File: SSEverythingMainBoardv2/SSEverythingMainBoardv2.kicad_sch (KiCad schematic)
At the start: 66 parts, among them J1 CONN_06SILK_FEMALE_PTH, J2 CONN_06SILK_FEMALE_PTH, J3 POWER, J4 Switch, J5 Conn_01x02, J6 Conn_01x05, M1 Left MOTOR, M2 Right MOTOR, Q1 PBSS4160DS, Q2 PBSS4160DS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

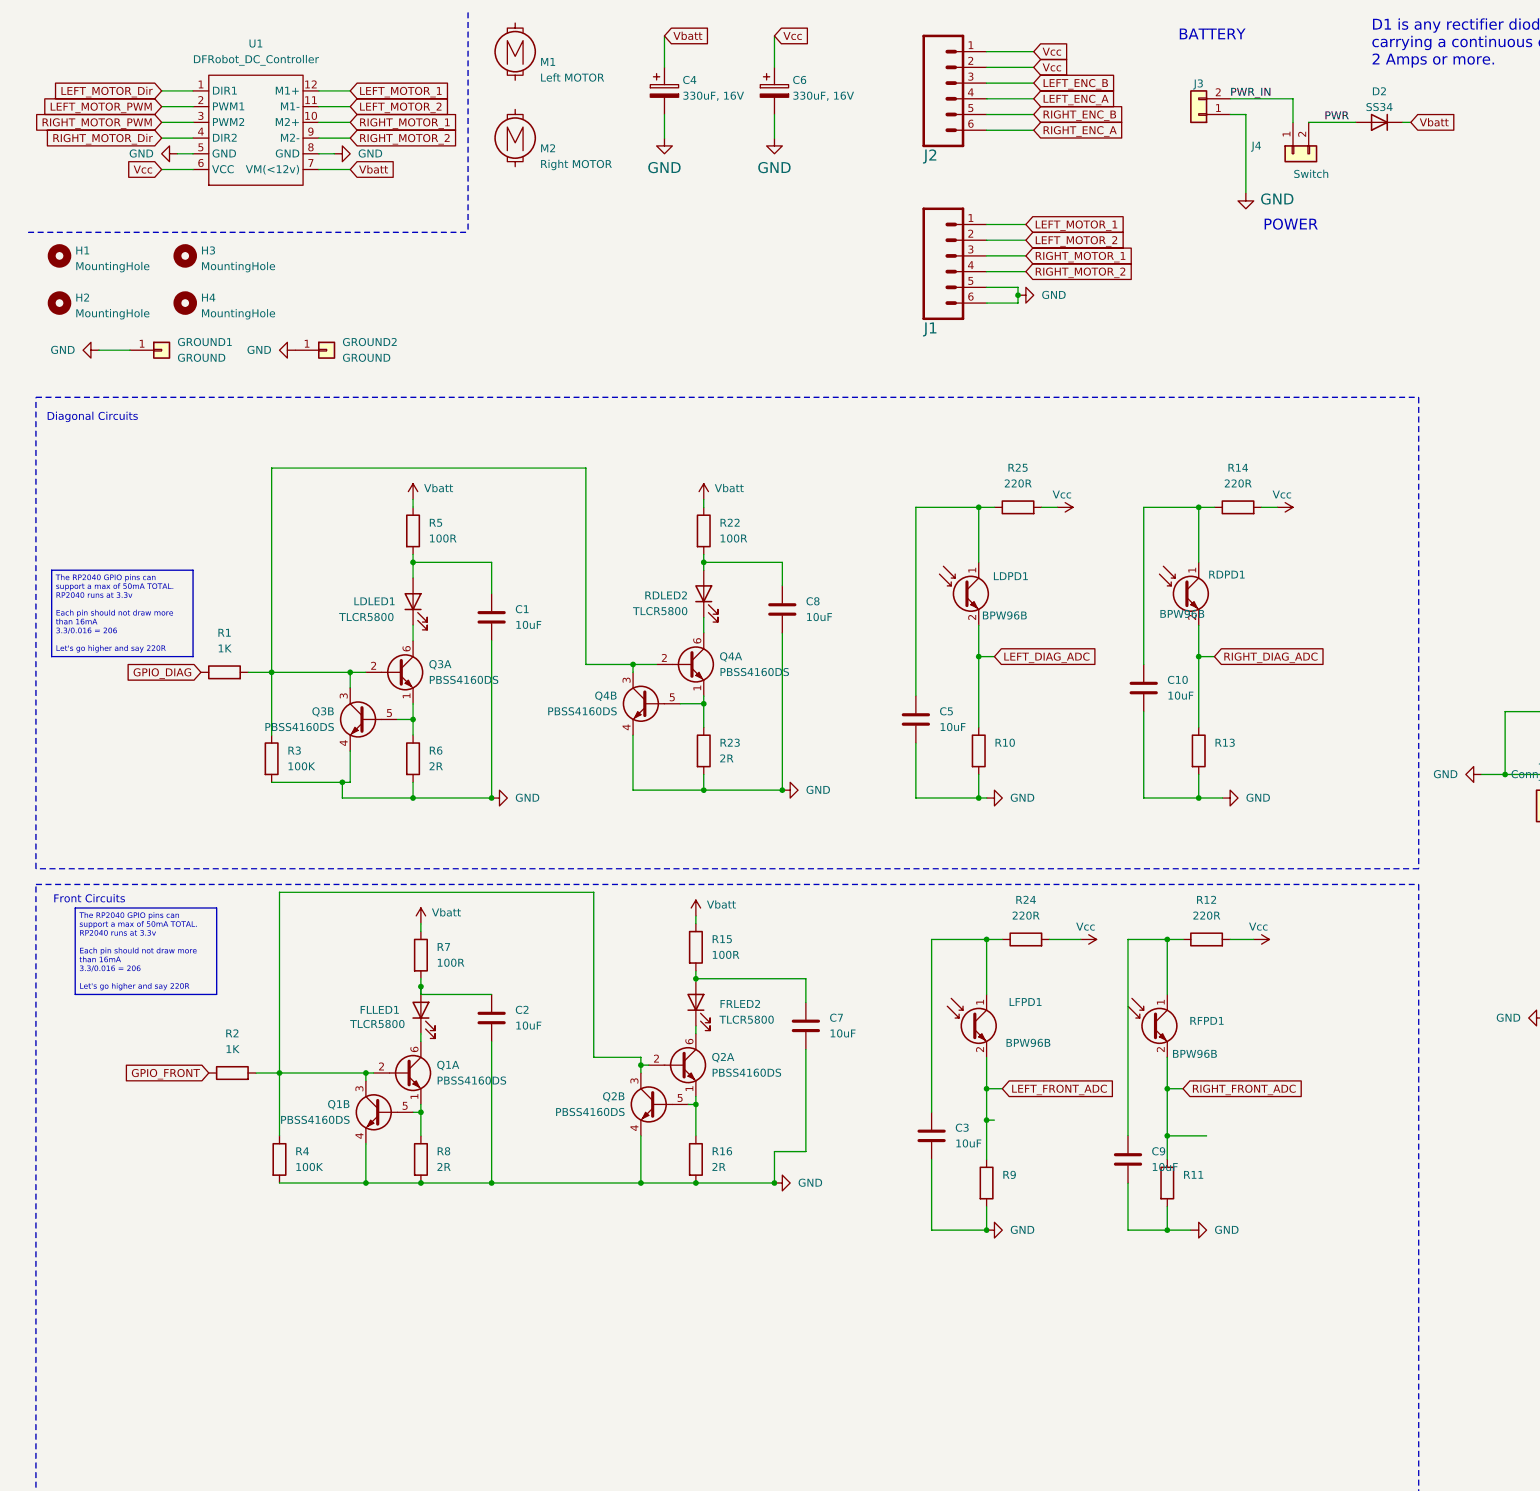
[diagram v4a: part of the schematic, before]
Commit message: updated sensor locations, all resistors are back to be 0805, routing changes and moved the motor controller around plus other changes from Peter's suggestions
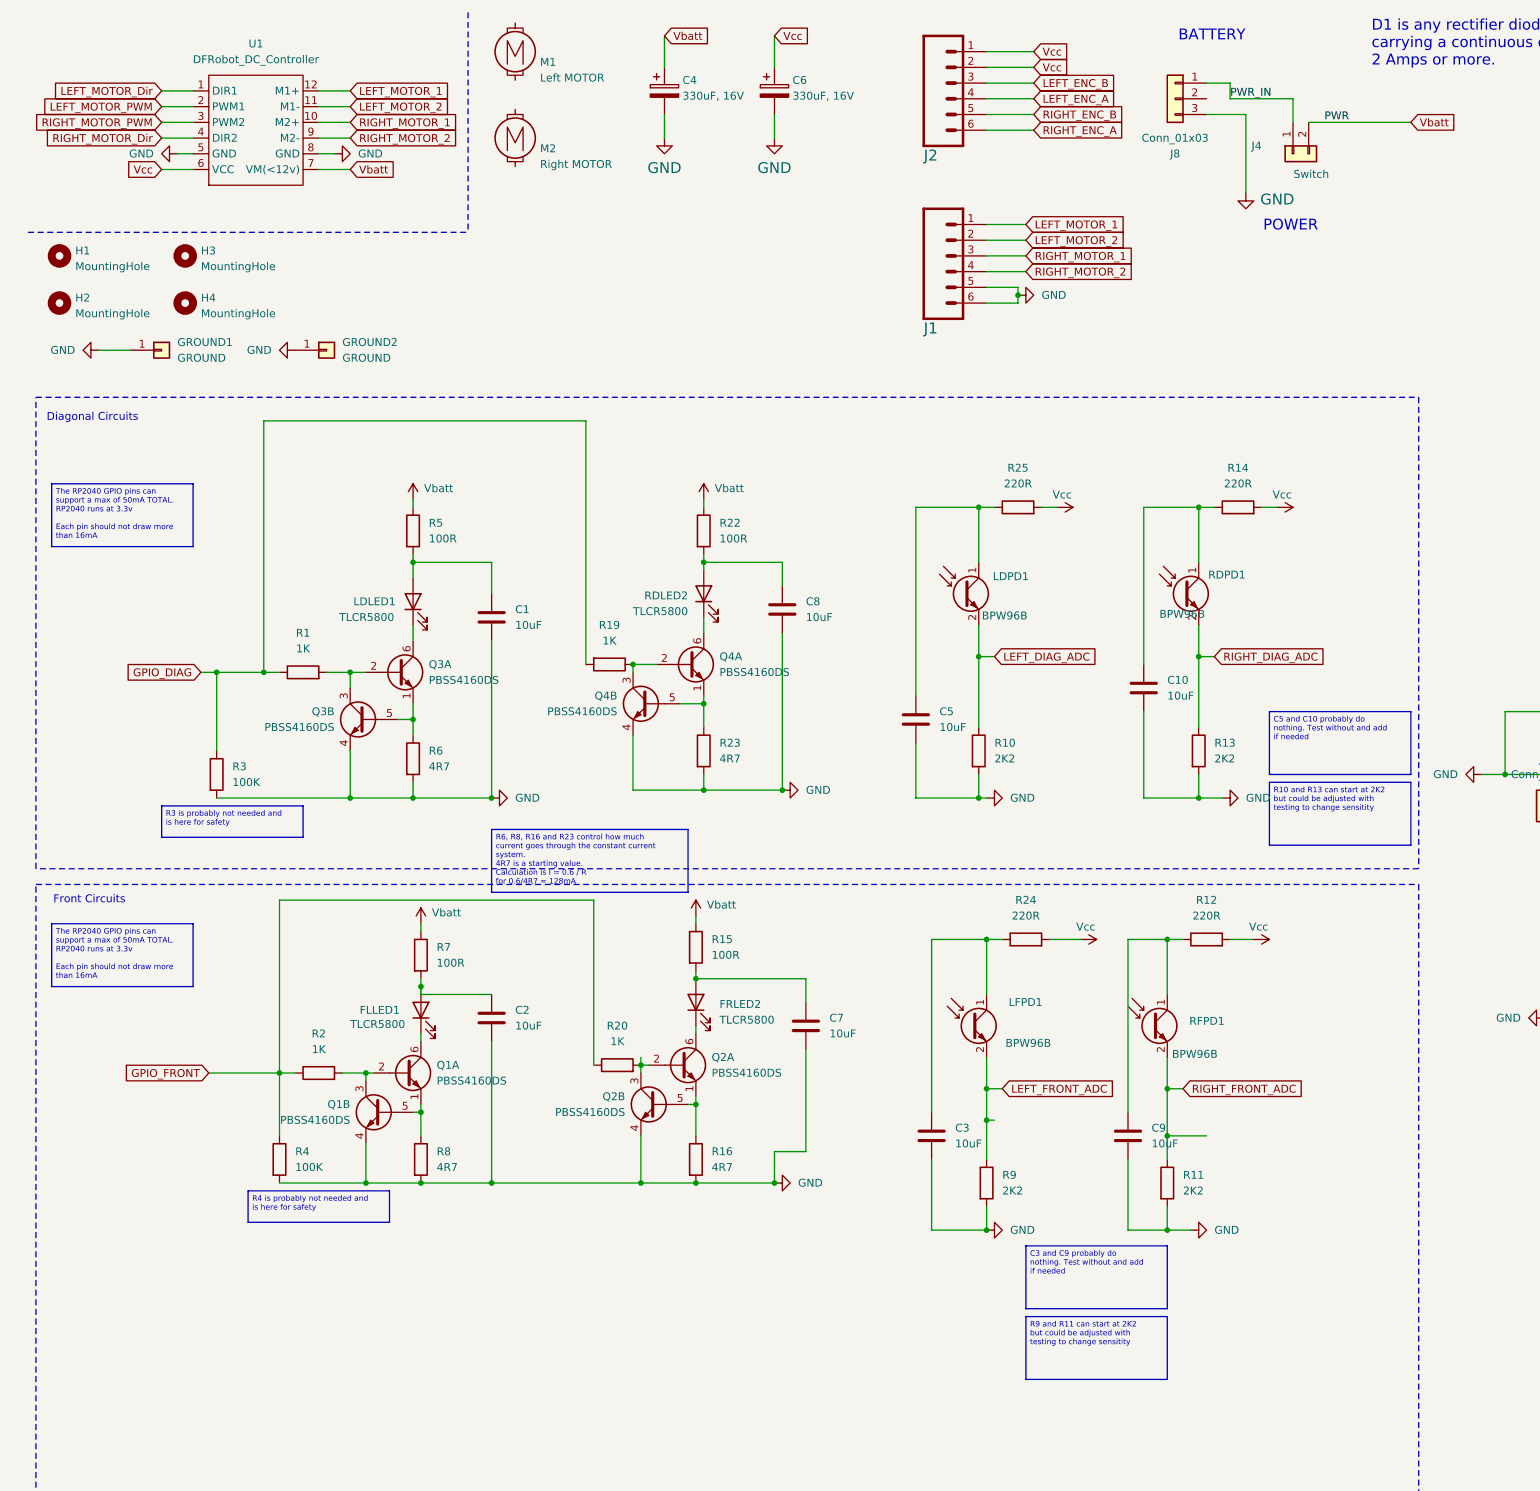
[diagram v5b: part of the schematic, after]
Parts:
- removed D2: SS34, Diode_SMD:D_SMC, symbol Device:D
- removed J3: POWER, Connector_PinHeader_2.54mm:PinHeader_1x02_P2.54mm_Vertical, symbol Connector_Generic:Conn_01x02
- added J8: Conn_01x03, Connector_JST:JST_XH_B3B-XH-A_1x03_P2.50mm_Vertical, symbol Connector_Generic:Conn_01x03
- added R19, R20: 1K, Resistor_SMD:R_0805_2012Metric_Pad1.20x1.40mm_HandSolder, symbol Device:R
- C4, C6: footprint Capacitor_THT:CP_Radial_D8.0mm_P2.50mm -> Capacitor_THT:C_Radial_D6.3mm_H7.0mm_P2.50mm
- R10, R11, R13, R9: value R -> 2K2
- R16, R23, R6, R8: value 2R -> 4R7; footprint Resistor_SMD:R_1206_3216Metric_Pad1.30x1.75mm_HandSolder -> Resistor_SMD:R_0805_2012Metric_Pad1.20x1.40mm_HandSolder
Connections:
- net PWR is gone; now on net Vbatt: J4.2 (Pin_2)
- net GND: now also J8.3 (Pin_3)
- net GPIO_DIAG: now also R3.1, R19.2
- net GPIO_FRONT: now also R4.1, R20.1
- net PWR_IN: now also J8.1 (Pin_1)
- net at Q1.2 (B1), Q1.3 (C2), R2.2: no longer Q2.2 (B1), Q2.3 (C2), R4.1
- net at Q3.2 (B1), Q3.3 (C2), R1.2: no longer Q4.2 (B1), Q4.3 (C2), R3.1
- new net: Q4.2 (B1), Q4.3 (C2), R19.1
- new net: Q2.2 (B1), Q2.3 (C2), R20.2
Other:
- moved on the sheet: C9, R1, R2, R3

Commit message: routing changes
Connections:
- net LEFT_DIAG_ADC: now also A1.19 (A0); no longer A1.20 (A1)
- net LEFT_FRONT_ADC: now also A1.20 (A1); no longer A1.19 (A0)

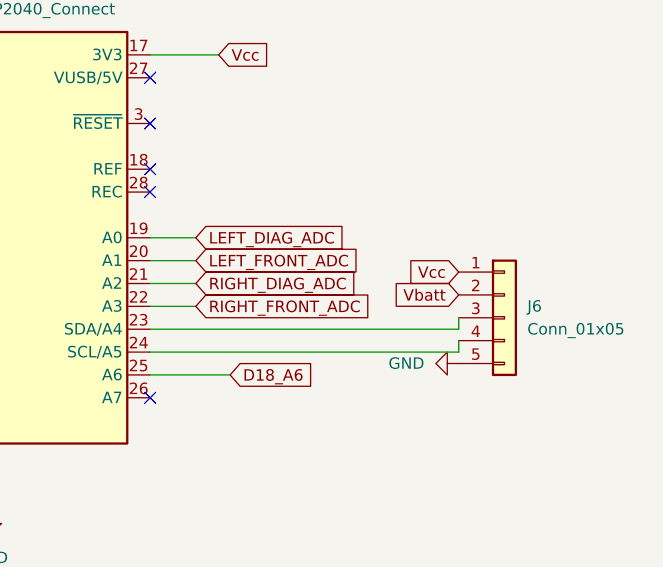
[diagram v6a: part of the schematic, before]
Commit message: New board sent to JLCPCB for new Chassis
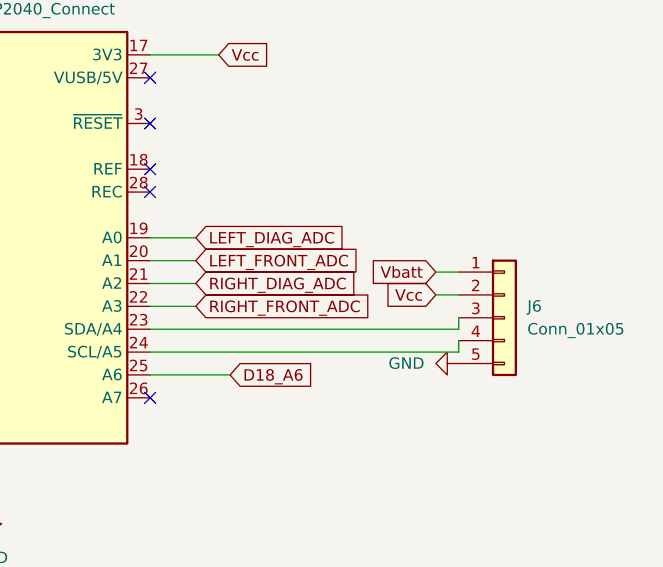
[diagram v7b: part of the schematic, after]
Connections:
- net Vbatt: now also J6.1 (Pin_1); no longer J6.2 (Pin_2)
- net Vcc: now also J6.2 (Pin_2); no longer J6.1 (Pin_1)
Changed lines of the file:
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@@
+	(wire
+		(pts
+			(xy 364.49 160.02) (xy 367.03 160.02)
+		)
+		(stroke
+			(width 0)
+			(type default)
+		)
+	)
 	(wire
 		(pts
@@
 		(pts
 			(xy 110.49 118.11) (xy 110.49 119.38)
+		)
+		(stroke
+			(width 0)
+			(type default)
+		)
+	)
+	(wire
+		(pts
+			(xy 364.49 162.56) (xy 367.03 162.56)
 		)
 		(stroke
@@
 	(global_label "Vcc"
 		(shape input)
-		(at 367.03 160.02 180)
+		(at 364.49 162.56 180)
 		(fields_autoplaced yes)
 		(effects
@@
 		)
 		(property "Intersheetrefs" "${INTERSHEET_REFS}"
-			(at 360.779 160.02 0)
+			(at 358.239 162.56 0)
 			(effects
 				(font
@@
 	(global_label "Vbatt"
 		(shape input)
-		(at 367.03 162.56 180)
+		(at 364.49 160.02 180)
 		(fields_autoplaced yes)
 		(effects
@@
 		)
 		(property "Intersheetrefs" "${INTERSHEET_REFS}"
-			(at 359.2068 162.56 0)
-			(effects
-				(font
+			(at 356.6668 160.02 0)
+			(effects
+				(font
